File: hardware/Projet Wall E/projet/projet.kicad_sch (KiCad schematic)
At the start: 0 parts

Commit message: Mise à jour alim, moteur et schéma principal
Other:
- sheet Alimentation ports: added CHG_PG, USB_DM, USB_DP; removed 5V_MOT, VSYS
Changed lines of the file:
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@@
 		)
 		(pin "CHG_INT" output
+			(at 100.33 50.8 0)
+			(effects
+				(font
+					(size 1.27 1.27)
+				)
+				(justify right)
+			)
+		)
+		(pin "CHG_OTG" output
 			(at 100.33 53.34 0)
 			(effects
@@
 			)
 		)
-		(pin "CHG_OTG" output
+		(pin "CHG_PG" output
+			(at 100.33 55.88 0)
+			(effects
+				(font
+					(size 1.27 1.27)
+				)
+				(justify right)
+			)
+		)
+		(pin "GAUGE_INT" output
 			(at 100.33 58.42 0)
 			(effects
@@
 		)
 		(pin "SCL" input
-			(at 100.33 63.5 0)
+			(at 100.33 66.04 0)
 			(effects
 				(font
@@
 		)
 		(pin "SDA" bidirectional
-			(at 100.33 69.85 0)
+			(at 100.33 68.58 0)
 			(effects
 				(font
@@
 			)
 		)
-		(pin "5V_MOT" output
-			(at 100.33 74.93 0)
+		(pin "USB_DM" bidirectional
+			(at 100.33 73.66 0)
 			(effects
 				(font
@@
 			)
 		)
-		(pin "VSYS" passive
-			(at 100.33 78.74 0)
+		(pin "USB_DP" bidirectional
+			(at 100.33 76.2 0)
 			(effects
 				(font
-					(size 1.27 1.27)
-				)
-				(justify right)
-			)
-		)
-		(pin "GAUGE_INT" output
-			(at 100.33 85.09 0)
-			(effects
-				(font

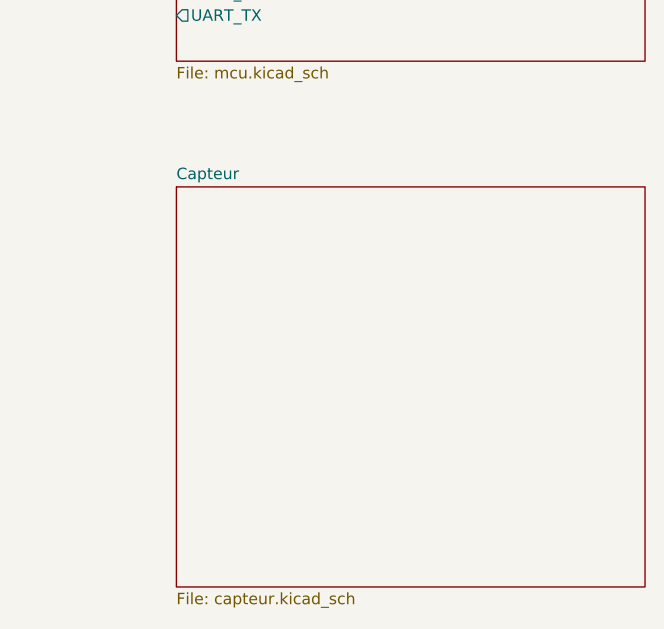
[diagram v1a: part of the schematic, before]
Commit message: feat: mise a jour capteur et projet: empreintes
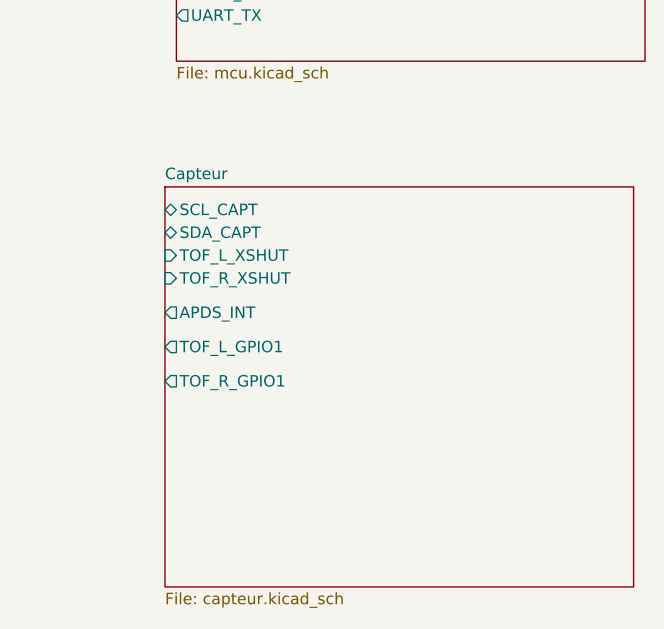
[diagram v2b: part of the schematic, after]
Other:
- sheet Capteur ports: added APDS_INT, SCL_CAPT, SDA_CAPT, TOF_L_GPIO1, TOF_L_XSHUT, TOF_R_GPIO1, TOF_R_XSHUT; removed none
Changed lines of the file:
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@@
 	(paper "A4")
 	(sheet
-		(at 125.73 102.87)
+		(at 124.46 102.87)
 		(size 52.07 44.45)
 		(exclude_from_sim no)
@@
 		)
 		(property "Sheetname" "Capteur"
-			(at 125.73 102.1584 0)
+			(at 124.46 102.1584 0)
 			(show_name no)
 			(do_not_autoplace no)
@@
 		)
 		(property "Sheetfile" "capteur.kicad_sch"
-			(at 125.73 147.9046 0)
+			(at 124.46 147.9046 0)
 			(show_name no)
 			(do_not_autoplace no)
@@
 			)
 		)
+		(pin "SCL_CAPT" bidirectional
+			(at 124.46 105.41 180)
+			(effects
+				(font
+					(size 1.27 1.27)
+				)
+				(justify left)
+			)
+		)
+		(pin "SDA_CAPT" bidirectional
+			(at 124.46 107.95 180)
+			(effects
+				(font
+					(size 1.27 1.27)
+				)
+				(justify left)
+			)
+		)
+		(pin "TOF_L_XSHUT" input
+			(at 124.46 110.49 180)
+			(effects
+				(font
+					(size 1.27 1.27)
+				)
+				(justify left)
+			)
+		)
+		(pin "TOF_R_XSHUT" input
+			(at 124.46 113.03 180)
+			(effects
+				(font
+					(size 1.27 1.27)
+				)
+				(justify left)
+			)
+		)
+		(pin "APDS_INT" output
+			(at 124.46 116.84 180)
+			(effects
+				(font
+					(size 1.27 1.27)
+				)
+				(justify left)
+			)
+		)
+		(pin "TOF_L_GPIO1" output
+			(at 124.46 120.65 180)
+			(effects
+				(font
+					(size 1.27 1.27)
+				)
+				(justify left)
+			)
+		)
+		(pin "TOF_R_GPIO1" output
+			(at 124.46 124.46 180)
+			(effects
+				(font
+					(size 1.27 1.27)
+				)
+				(justify left)
+			)
+		)
